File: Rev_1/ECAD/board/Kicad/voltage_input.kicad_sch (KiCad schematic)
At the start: 21 parts, among them Q1 PMOS, Q2 PNP, Q3 PNP

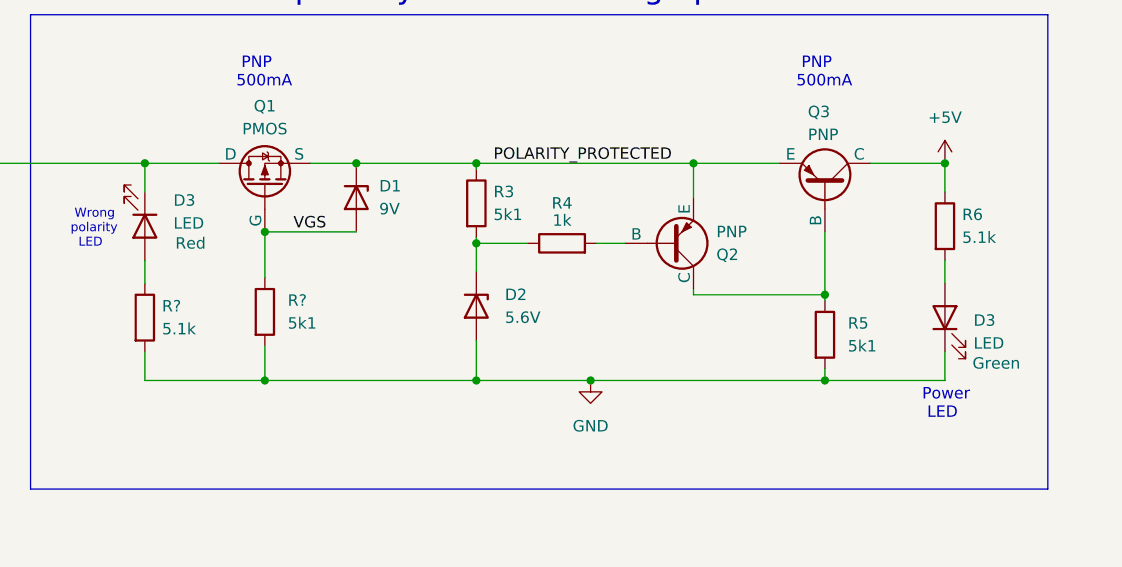
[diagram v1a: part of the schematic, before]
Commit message: Added Rotary encoder and buttons to the Input Buffer
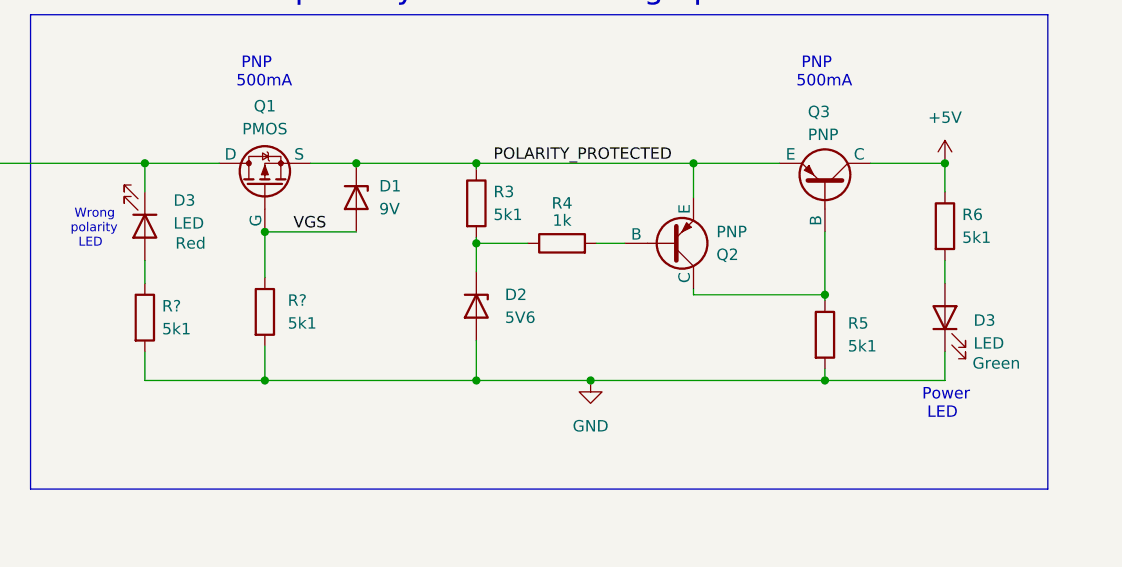
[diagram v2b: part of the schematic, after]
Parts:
- D2: value 5.6V -> 5V6
- R6, R?: value 5.1k -> 5k1
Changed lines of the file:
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@@
       (effects (font (size 1.27 1.27)) (justify left))
     )
-    (property "Value" "5.1k" (at 135.89 112.395 0)
+    (property "Value" "5k1" (at 135.89 112.395 0)
       (effects (font (size 1.27 1.27)) (justify left))
     )
@@
       (effects (font (size 1.27 1.27)) (justify left))
     )
-    (property "Value" "5.1k" (at 224.79 102.235 0)
+    (property "Value" "5k1" (at 224.79 102.235 0)
       (effects (font (size 1.27 1.27)) (justify left))
     )
@@
       (effects (font (size 1.27 1.27)) (justify left))
     )
-    (property "Value" "5.6V" (at 173.99 111.125 90)
-      (effects (font (size 1.27 1.27)) (justify left))
-    )
+    (property "Value" "5V6" (at 173.99 111.125 90)
+      (effects (font (size 1.27 1.27)) (justify left))
+    )

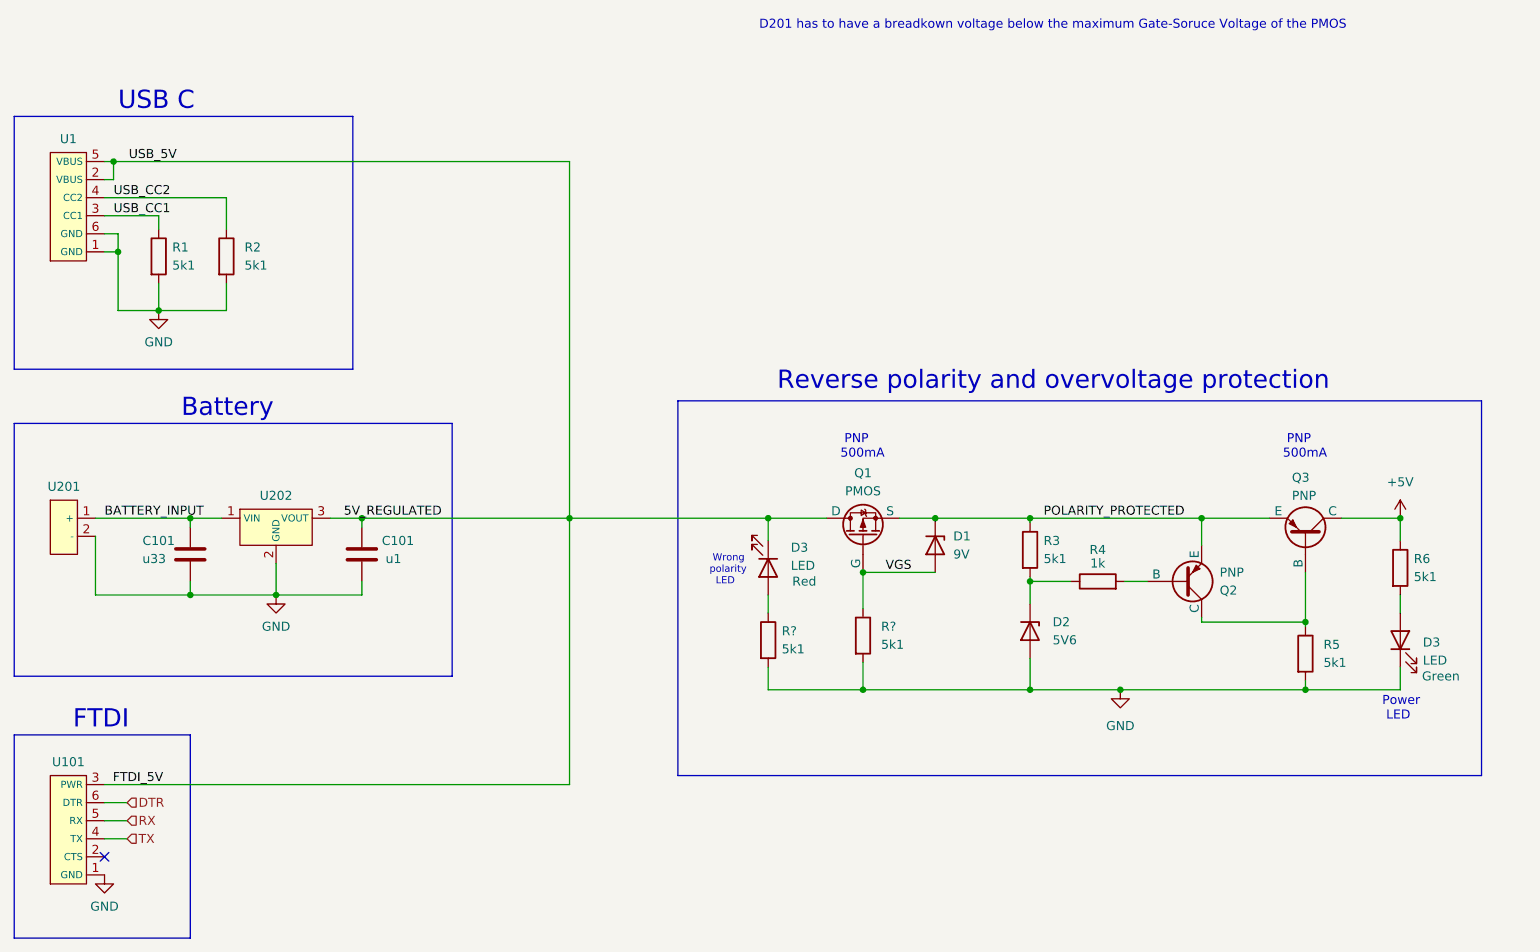
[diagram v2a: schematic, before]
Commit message: Updated gitignore
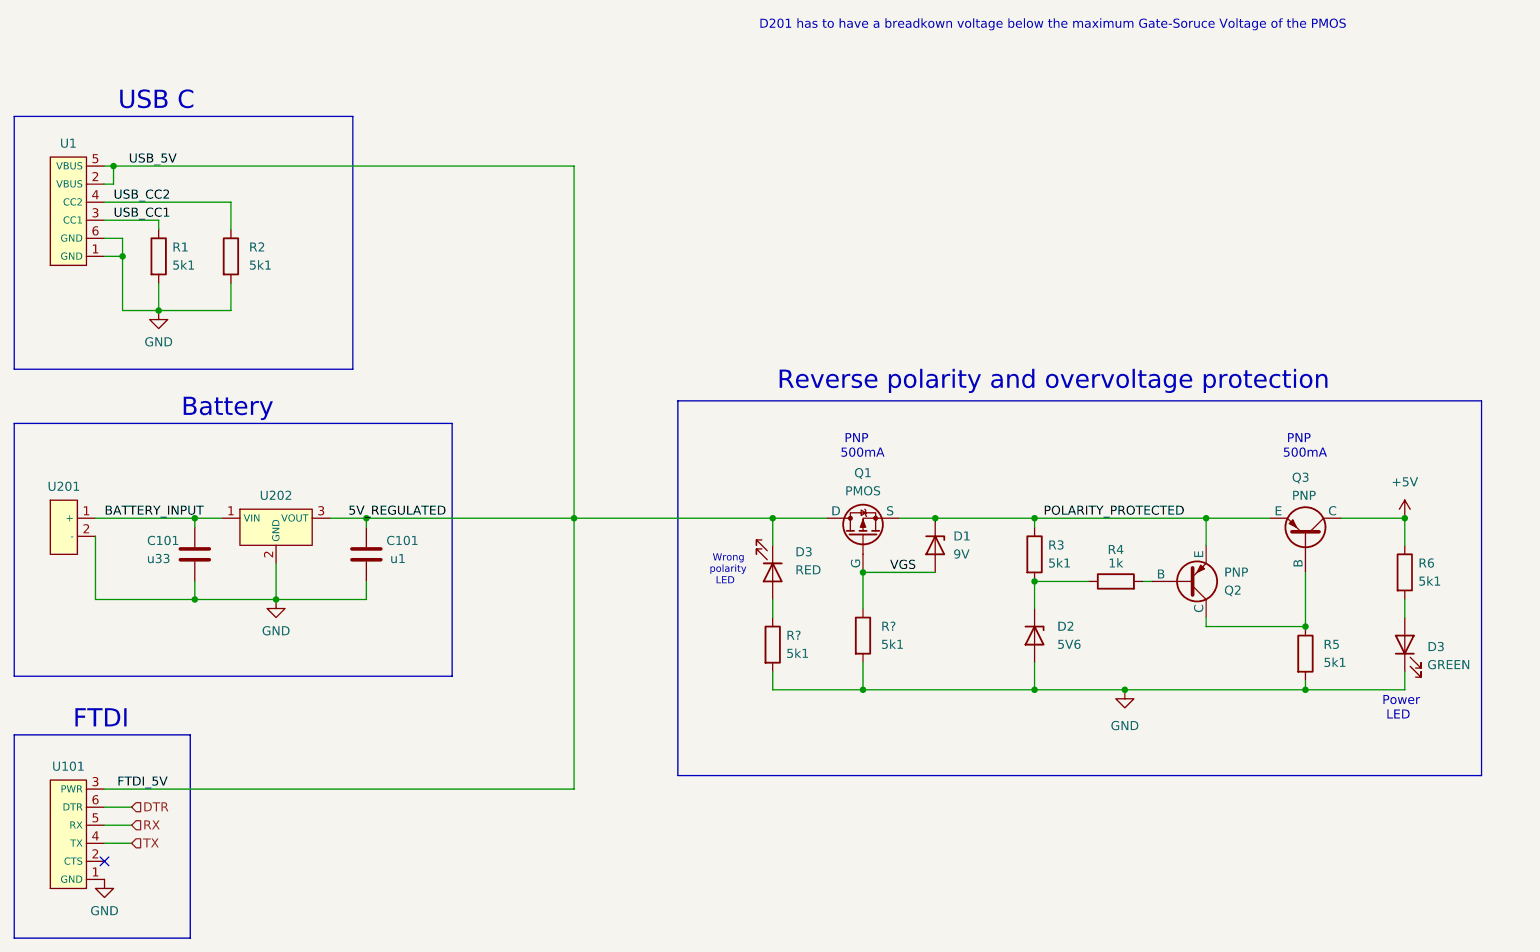
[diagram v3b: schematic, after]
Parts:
- D3: value LED -> RED; Color Red -> (none)
- D3: value LED -> GREEN; Color Green -> (none)
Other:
- moved on the sheet: C101, D2, D3, Q2, R2, R3, R4, R6, R?, U1, U101
